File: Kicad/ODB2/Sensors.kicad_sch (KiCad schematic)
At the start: 17 parts, among them J4 RF2-04A-T-00-50-G, U5 L76L-M33, U6 ICM-20948, U7 MS580301BA01-00

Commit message: led
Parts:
- LED_BT1: value BT_LED1_G -> LED1_B
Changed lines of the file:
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@@
 			)
 		)
-		(property "Value" "BT_LED1_G"
+		(property "Value" "LED1_B"
 			(at 227.584 53.594 0)
 			(effects

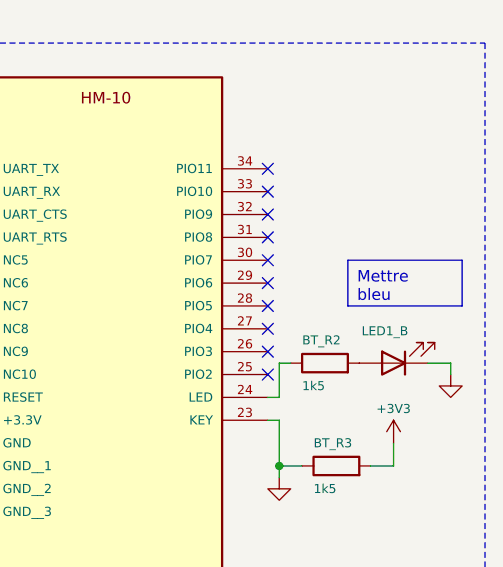
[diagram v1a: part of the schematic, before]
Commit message: ajustement resistances et pyro_test 2e iteration
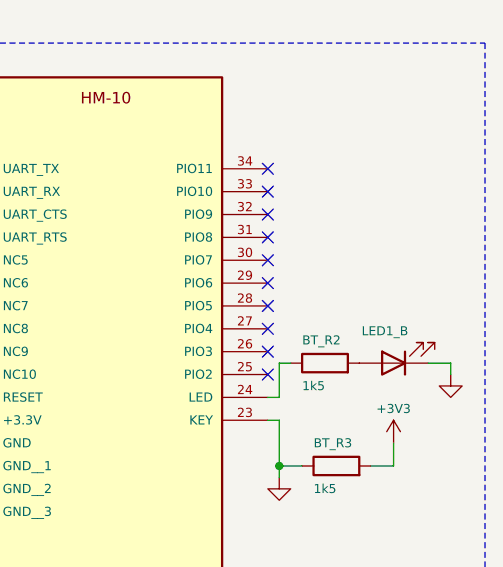
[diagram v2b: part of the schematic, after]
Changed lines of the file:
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@@
-		)
-	)
-	(text_box "Mettre bleu"
-		(exclude_from_sim no)
-		(at 226.06 45.72 0)
-		(size 12.7 5.08)
-		(stroke
-			(width 0)
-			(type default)
-		)
-		(fill
-			(type none)
-		)
-		(effects
-			(font
-				(size 1.27 1.27)
-			)
-			(justify left top)
 		)
 	)

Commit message: fixes merge
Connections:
- net SPI4_Baro_CS: now also U7.8 (CSB)
- net SPI4_Baro_MISO: now also U7.6 (SDO)
- net SPI4_Baro_MOSI: now also U7.5 (SDI\SDA)
- net SPI4_Baro_SCLK: now also U7.7 (SCLK)
- no-connect marks 32 -> 33
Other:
- moved on the sheet: BT_C1
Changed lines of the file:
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@@
+	)
+	(junction
+		(at 154.94 63.5)
+		(diameter 0)
+		(color 0 0 0 0)
 	)
 	(junction
@@
 	)
 	(junction
-		(at 154.94 62.23)
-		(diameter 0)
-		(color 0 0 0 0)
-	)
-	(junction
 		(at 29.21 46.99)
 		(diameter 0)
@@
 	)
 	(no_connect
+		(at 78.74 132.08)
+	)
+	(no_connect
 		(at 200.66 93.98)
 	)
@@
 	(wire
 		(pts
+			(xy 33.02 127) (xy 34.29 127)
+		)
+		(stroke
+			(width 0)
+			(type default)
+		)
+	)
+	(wire
+		(pts
 			(xy 127 44.45) (xy 130.81 44.45)
 		)
@@
 	(wire
 		(pts
+			(xy 33.02 129.54) (xy 34.29 129.54)
+		)
+		(stroke
+			(width 0)
+			(type default)
+		)
+	)
+	(wire
+		(pts
 			(xy 218.44 60.96) (xy 217.17 60.96)
 		)
@@
 	(wire
 		(pts
+			(xy 33.02 124.46) (xy 34.29 124.46)
+		)
+		(stroke
+			(width 0)
+			(type default)
+		)
+	)
+	(wire
+		(pts
 			(xy 105.41 49.53) (xy 116.84 49.53)
 		)
@@
 	(wire
 		(pts
-			(xy 154.94 59.69) (xy 154.94 62.23)
-		)
-		(stroke
-			(width 0)
-			(type default)
-		)
-	)
-	(wire
-		(pts
 			(xy 78.74 124.46) (xy 81.28 124.46)
 		)
@@
 	(wire
 		(pts
+			(xy 33.02 132.08) (xy 34.29 132.08)
+		)
+		(stroke
+			(width 0)
+			(type default)
+		)
+	)
+	(wire
+		(pts
 			(xy 17.78 101.6) (xy 17.78 105.41)
 		)
@@
 	(wire
 		(pts
-			(xy 154.94 69.85) (xy 154.94 73.66)
+			(xy 154.94 71.12) (xy 154.94 73.66)
 		)
 		(stroke
@@
 	(wire
 		(pts
-			(xy 154.94 62.23) (xy 154.94 63.5)
+			(xy 154.94 59.69) (xy 154.94 63.5)
 		)
 		(stroke
@@
 	(symbol
 		(lib_id "Device:C")
-		(at 154.94 66.04 0)
+		(at 154.94 67.31 0)
 		(unit 1)
 		(exclude_from_sim no)
@@
 		(dnp no)
 		(property "Reference" "BT_C1"
-			(at 158.496 66.294 0)
+			(at 158.496 67.564 0)
 			(effects
 				(font
@@
 		)
 		(property "Value" "10uF"
-			(at 158.496 68.072 0)
+			(at 158.496 69.342 0)
 			(effects
 				(font
@@
 		)
 		(property "Footprint" ""
-			(at 155.9052 69.85 0)
+			(at 155.9052 71.12 0)
 			(effects
 				(font
@@
 		)
 		(property "Datasheet" "~"
-			(at 154.94 66.04 0)
+			(at 154.94 67.31 0)
 			(effects
 				(font
@@
 		)
 		(property "Description" "Unpolarized capacitor"
-			(at 154.94 66.04 0)
-			(effects
-				(font
+			(at 154.94 67.31 0)
+			(effects
+				(font

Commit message: footprint
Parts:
- BT_C1, BT_C2, Baro_C1, GPS_C1, ICM_C1, ICM_C2: footprint (none) -> Capacitor_SMD:C_0805_2012Metric
- BT_R1: footprint (none) -> Resistor_SMD:R_0805_2012Metric
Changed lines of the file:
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@@
 			)
 		)
-		(property "Footprint" ""
+		(property "Footprint" "Resistor_SMD:R_0805_2012Metric"
 			(at 161.29 57.912 90)
 			(effects
@@
 			)
 		)
-		(property "Footprint" ""
+		(property "Footprint" "Capacitor_SMD:C_0805_2012Metric"
 			(at 27.94 53.6448 0)
 			(effects
@@
 			)
 		)
-		(property "Footprint" ""
+		(property "Footprint" "Capacitor_SMD:C_0805_2012Metric"
 			(at 155.9052 71.12 0)
 			(effects
@@
 			)
 		)
-		(property "Footprint" ""
+		(property "Footprint" "Capacitor_SMD:C_0805_2012Metric"
 			(at 169.8752 72.39 0)
 			(effects
@@
 			)
 		)
-		(property "Footprint" ""
+		(property "Footprint" "Capacitor_SMD:C_0805_2012Metric"
 			(at 21.59 100.0252 0)
 			(effects
@@
 			)
 		)
-		(property "Footprint" ""
+		(property "Footprint" "Capacitor_SMD:C_0805_2012Metric"
 			(at 83.82 123.4948 0)
 			(effects
@@
 			)
 		)
-		(property "Footprint" ""
+		(property "Footprint" "Capacitor_SMD:C_0805_2012Metric"
 			(at 108.2548 93.98 0)
 			(effects

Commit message: fix and gate
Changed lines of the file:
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@@
 		)
 		(property "Value" "+3V3"
-			(at 154.686 52.578 0)
+			(at 154.432 52.07 0)
 			(effects
 				(font

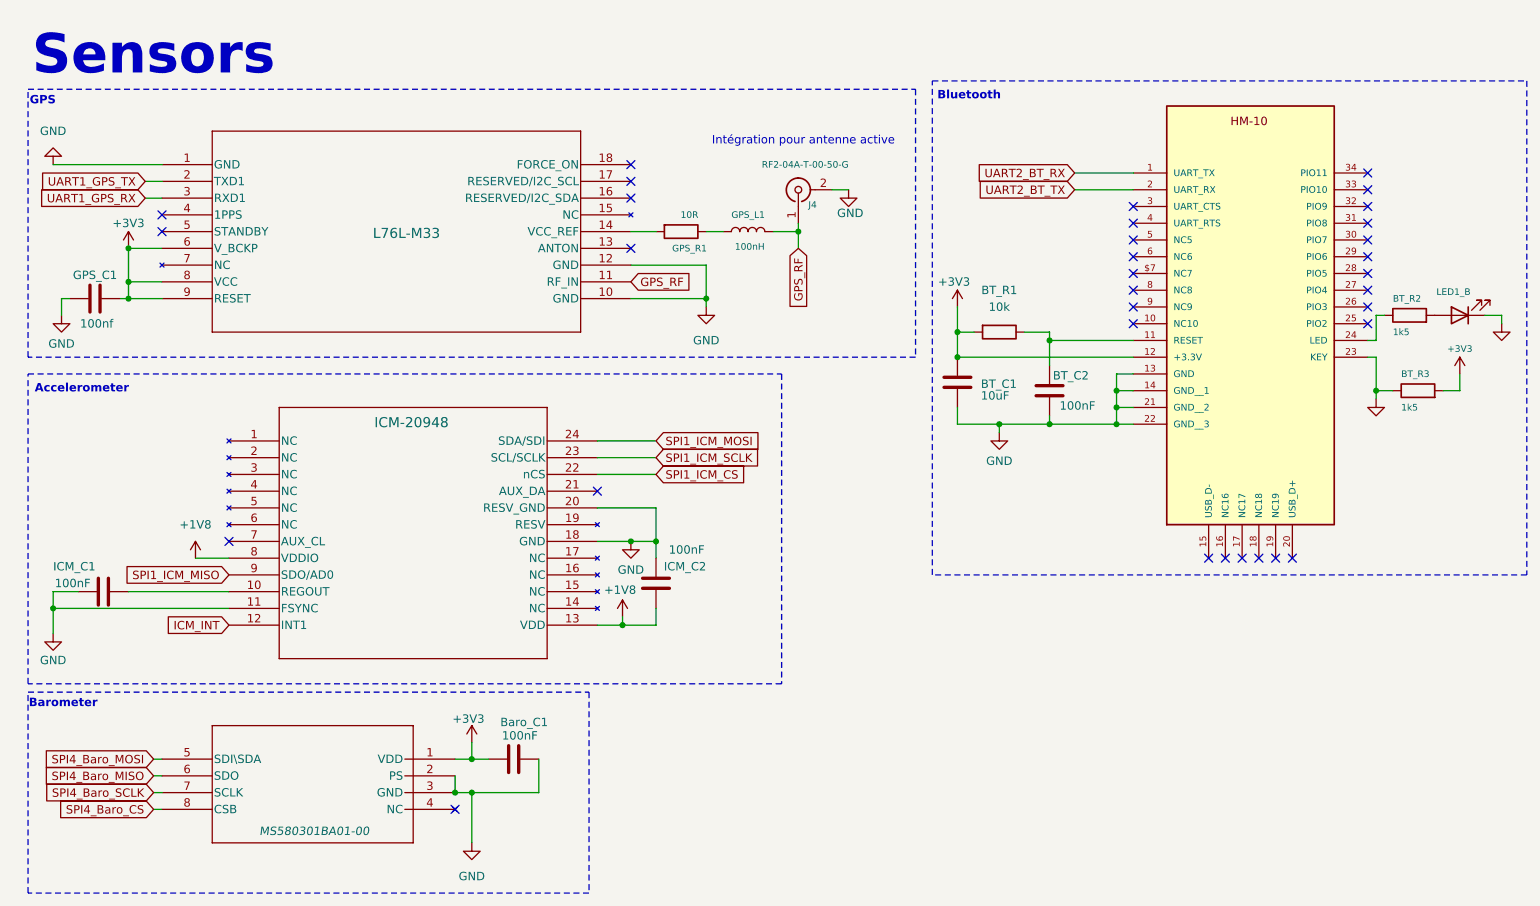
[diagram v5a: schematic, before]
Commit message: fix sw0 + merge acc/rfm + fix pdr_on
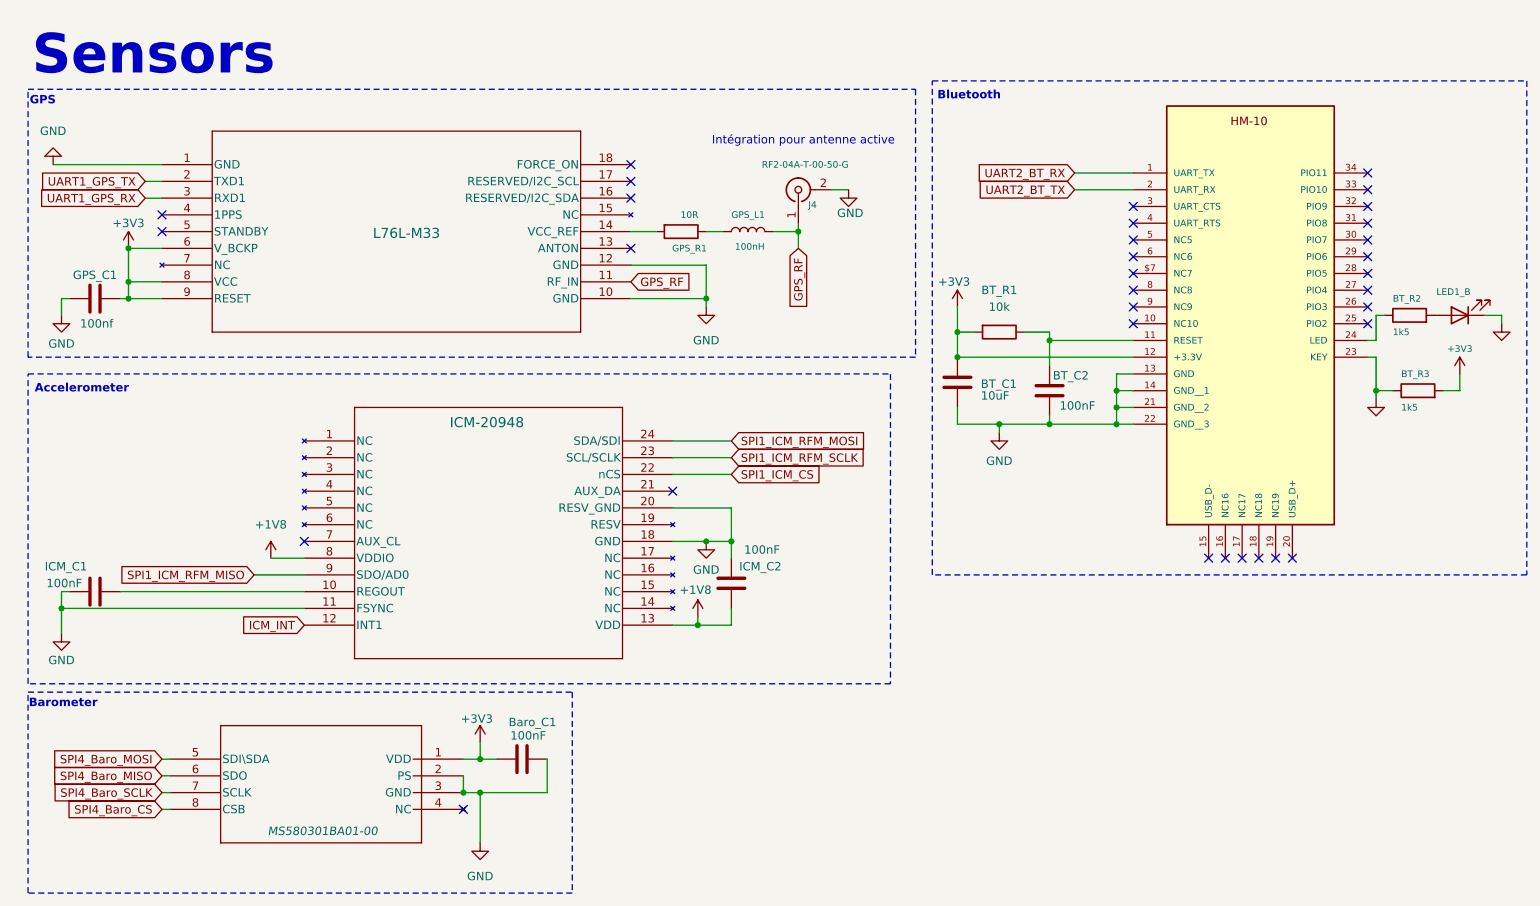
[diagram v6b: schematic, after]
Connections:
- net SPI1_ICM_MISO renamed SPI1_ICM_RFM_MISO
- net SPI1_ICM_MOSI renamed SPI1_ICM_RFM_MOSI
- net SPI1_ICM_SCLK renamed SPI1_ICM_RFM_SCLK
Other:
- moved on the sheet: Baro_C1, ICM_C1, ICM_C2

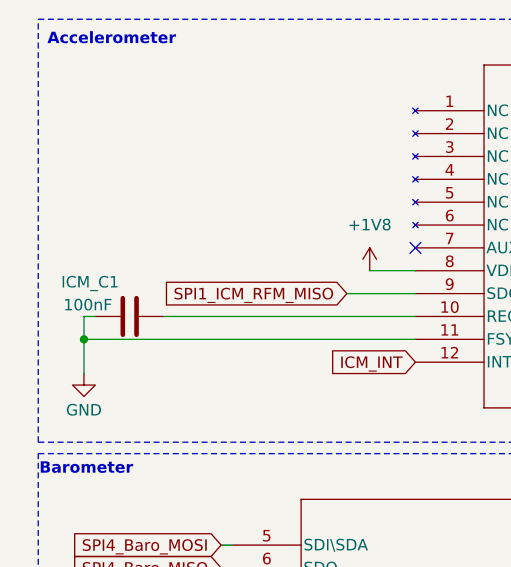
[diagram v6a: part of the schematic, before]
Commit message: fix 6v6Enable label
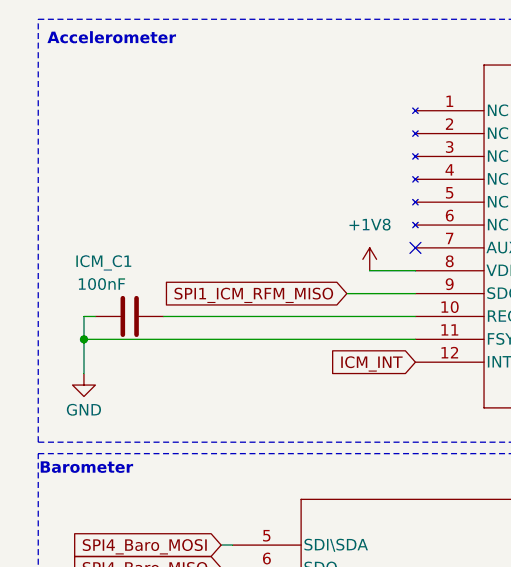
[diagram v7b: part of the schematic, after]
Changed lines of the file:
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@@
 		(dnp no)
 		(property "Reference" "ICM_C1"
-			(at 16.51 95.25 90)
+			(at 18.034 92.964 90)
 			(effects
 				(font
@@
 		)
 		(property "Value" "100nF"
-			(at 16.764 97.79 90)
+			(at 18.288 95.504 90)
 			(effects
 				(font

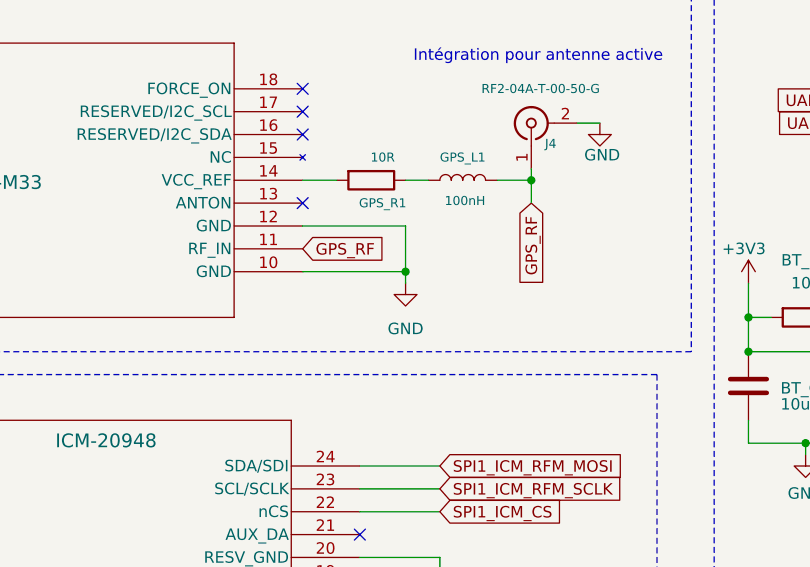
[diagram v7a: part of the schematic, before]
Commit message: Fix labels, 50 ohms, STM no connect
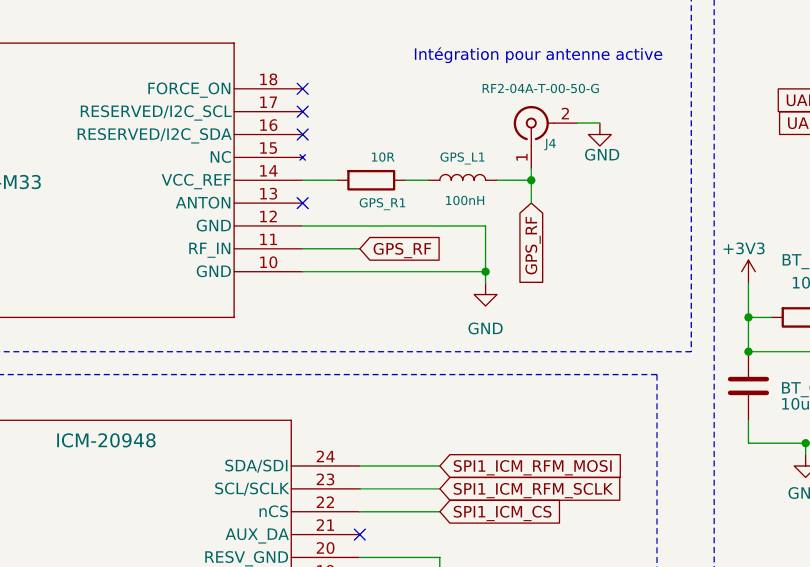
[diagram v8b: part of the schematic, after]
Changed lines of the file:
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@@
 	)
 	(junction
-		(at 116.84 54.61)
+		(at 125.73 54.61)
 		(diameter 0)
 		(color 0 0 0 0)
@@
 	(wire
 		(pts
-			(xy 116.84 49.53) (xy 116.84 54.61)
+			(xy 125.73 49.53) (xy 125.73 54.61)
 		)
 		(stroke
@@
 	(wire
 		(pts
-			(xy 116.84 55.88) (xy 116.84 54.61)
+			(xy 125.73 55.88) (xy 125.73 54.61)
 		)
 		(stroke
@@
 	(wire
 		(pts
-			(xy 105.41 49.53) (xy 116.84 49.53)
+			(xy 105.41 49.53) (xy 125.73 49.53)
 		)
 		(stroke
@@
 	(wire
 		(pts
-			(xy 105.41 54.61) (xy 116.84 54.61)
-		)
-		(stroke
-			(width 0)
-			(type default)
-		)
-	)
-	(wire
-		(pts
 			(xy 218.44 57.15) (xy 218.44 60.96)
 		)
@@
 	(wire
 		(pts
+			(xy 105.41 54.61) (xy 125.73 54.61)
+		)
+		(stroke
+			(width 0)
+			(type default)
+		)
+	)
+	(wire
+		(pts
 			(xy 80.01 124.46) (xy 82.55 124.46)
 		)
@@
 		(pts
 			(xy 111.76 104.14) (xy 115.57 104.14)
+		)
+		(stroke
+			(width 0)
+			(type default)
+		)
+	)
+	(wire
+		(pts
+			(xy 105.41 52.07) (xy 111.76 52.07)
 		)
 		(stroke
@@
 	(global_label "GPS_RF"
 		(shape input)
-		(at 105.41 52.07 0)
+		(at 111.76 52.07 0)
 		(fields_autoplaced yes)
 		(effects
@@
 		)
 		(property "Intersheetrefs" "${INTERSHEET_REFS}"
-			(at 115.4709 52.07 0)
+			(at 121.8209 52.07 0)
 			(effects
 				(font
@@
 				(justify left)
 				(hide yes)
+			)
+		)
+	)
+	(netclass_flag ""
+		(length 2.54)
+		(shape round)
+		(at 110.49 52.07 0)
+		(effects
+			(font
+				(size 1.27 1.27)
+			)
+			(justify left bottom)
+		)
+		(property "50 ohm" "50 ohm"
+			(at 102.362 50.546 0)
+			(effects
+				(font
+					(size 1.27 1.27)
+					(italic yes)
+				)
+				(justify left)
 			)
 		)
@@
 	(symbol
 		(lib_id "power:GND")
-		(at 116.84 55.88 0)
+		(at 125.73 55.88 0)
 		(unit 1)
 		(exclude_from_sim no)
@@
 		(fields_autoplaced yes)
 		(property "Reference" "#PWR051"
-			(at 116.84 62.23 0)
+			(at 125.73 62.23 0)
 			(effects
 				(font
@@
 		)
 		(property "Value" "GND"
-			(at 116.84 60.96 0)
+			(at 125.73 60.96 0)
 			(effects
 				(font
@@
 		)
 		(property "Footprint" ""
-			(at 116.84 55.88 0)
+			(at 125.73 55.88 0)
 			(effects
 				(font
@@
 		)
 		(property "Datasheet" ""
-			(at 116.84 55.88 0)
+			(at 125.73 55.88 0)
 			(effects
 				(font
@@
 		)
 		(property "Description" "Power symbol creates a global label with name \"GND\" , ground"
-			(at 116.84 55.88 0)
-			(effects
-				(font
+			(at 125.73 55.88 0)
+			(effects
+				(font
